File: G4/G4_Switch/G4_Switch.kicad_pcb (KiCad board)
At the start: 2 copper layers, 70.5 x 91.4 mm, 28 parts, among them J1 Conn_01x09_Socket, J2 Conn_01x09_Socket, J3 DB25_Plug, U1 NUCLEO-G491RE, U2 74HC594, U3 74HC594, U4 ULN2003A, U5 ULN2003A

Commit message: updated G4_Switch
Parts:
- added C1: C, Capacitor_THT:C_Disc_D3.4mm_W2.1mm_P2.50mm, F.Cu at (115.0, 95.2)
- added C2: C, Capacitor_THT:C_Disc_D3.4mm_W2.1mm_P2.50mm, F.Cu at (141.0, 99.1)
- added J_GNDA1: Conn_01x01_Female, Connector_PinHeader_2.54mm:PinHeader_1x01_P2.54mm_Vertical, F.Cu at (161.3, 54.6)
- U1: footprint G4Lib:MODULE_NUCLEO-G491RE20 -> G4Lib:MODULE_NUCLEO-G491RE20noar
- moved JP4 38.0 mm to (115.6, 83.8)
- moved JP9 18.0 mm to (151.8, 86.4)
- moved JP8 15.1 mm to (151.8, 92.1)
- moved U5 12.9 mm to (140.3, 64.8), turned to 90 degrees
- moved JP3 12.0 mm to (115.6, 80.0)
- moved U4 10.5 mm to (113.7, 64.8), turned to 90 degrees
- moved JP1 10.2 mm to (115.6, 90.2)
- moved U2 8.28 mm to (129.5, 95.2)
- moved U3 4.62 mm to (143.5, 95.2)
- moved J1 4.49 mm to (109.2, 49.5)
- moved R_IDENT1 4.26 mm to (151.8, 96.5), turned to -90 degrees
- moved R_LED10 3.18 mm to (135.3, 115.6)
- moved R_LED4 3.18 mm to (115.6, 115.6)
- moved R_LED8 3.18 mm to (128.9, 115.6)
- moved R_LED2 3.17 mm to (109.2, 115.6)
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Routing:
- net S_CLR: track 0.00 -> 75.1 mm
- net GS13: track 73.5 -> 131.8 mm
- net GS12: track 70.3 -> 127.2 mm
- net S_VALID: track 0.00 -> 54.1 mm
- net GS8: track 88.9 -> 120.3 mm
- net GS7: track 86.1 -> 116.6 mm
- net GS9: track 95.1 -> 124.1 mm
- net GS10: track 100.8 -> 128.2 mm
- net GS11: track 107.8 -> 133.6 mm
- net Net-(U2-QH'): track 0.00 -> 21.1 mm
- net Net-(U2-QH): track 0.00 -> 20.5 mm
- net 3V3: track 42.5 -> 62.7 mm
- net GS1: track 26.6 -> 8.41 mm
- net GS0: track 27.6 -> 9.94 mm
- net Net-(U2-QA): track 23.0 -> 38.2 mm
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- added copper zone on B.Cu, net GND
- added copper zone on B.Cu, net GNDA
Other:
- board text added: "G4 Switch V1.0"
- board text removed: "Template G4 V2"

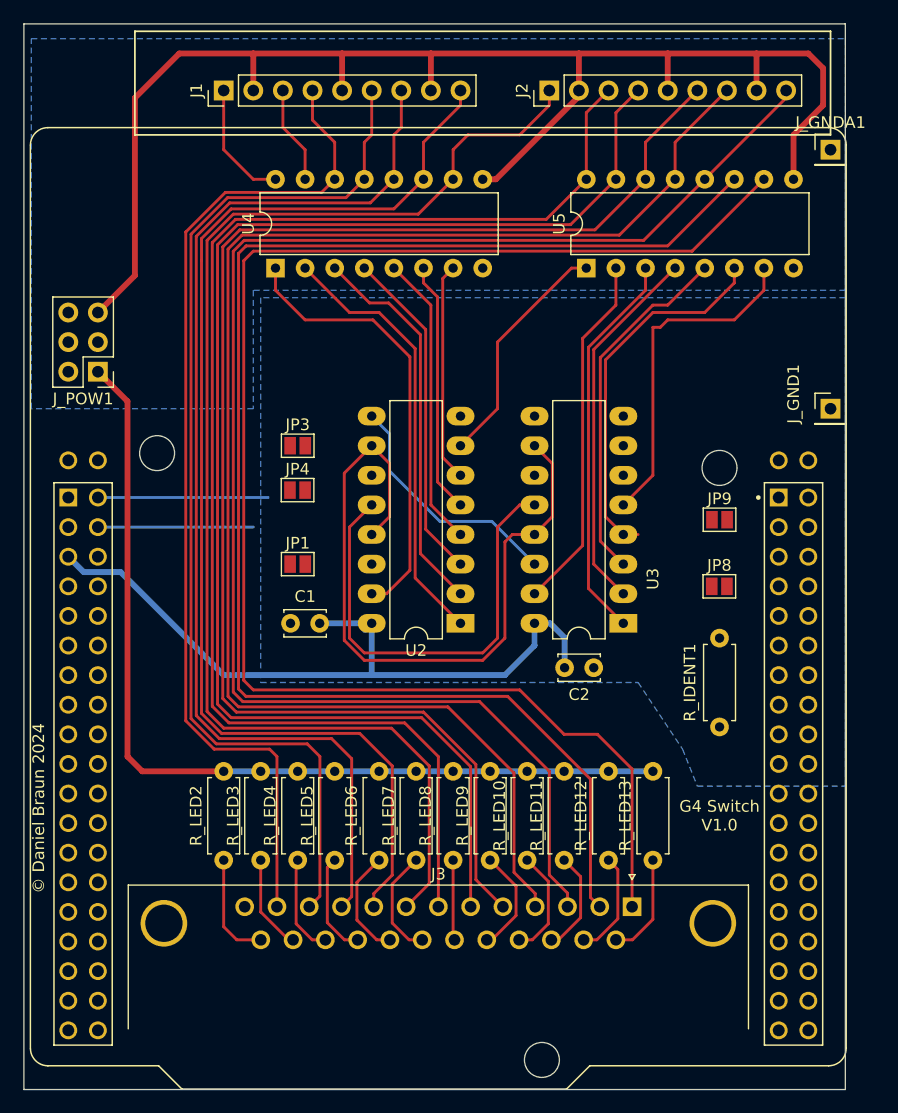
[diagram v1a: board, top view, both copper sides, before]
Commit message: updated G4_Switch, DRC run ok
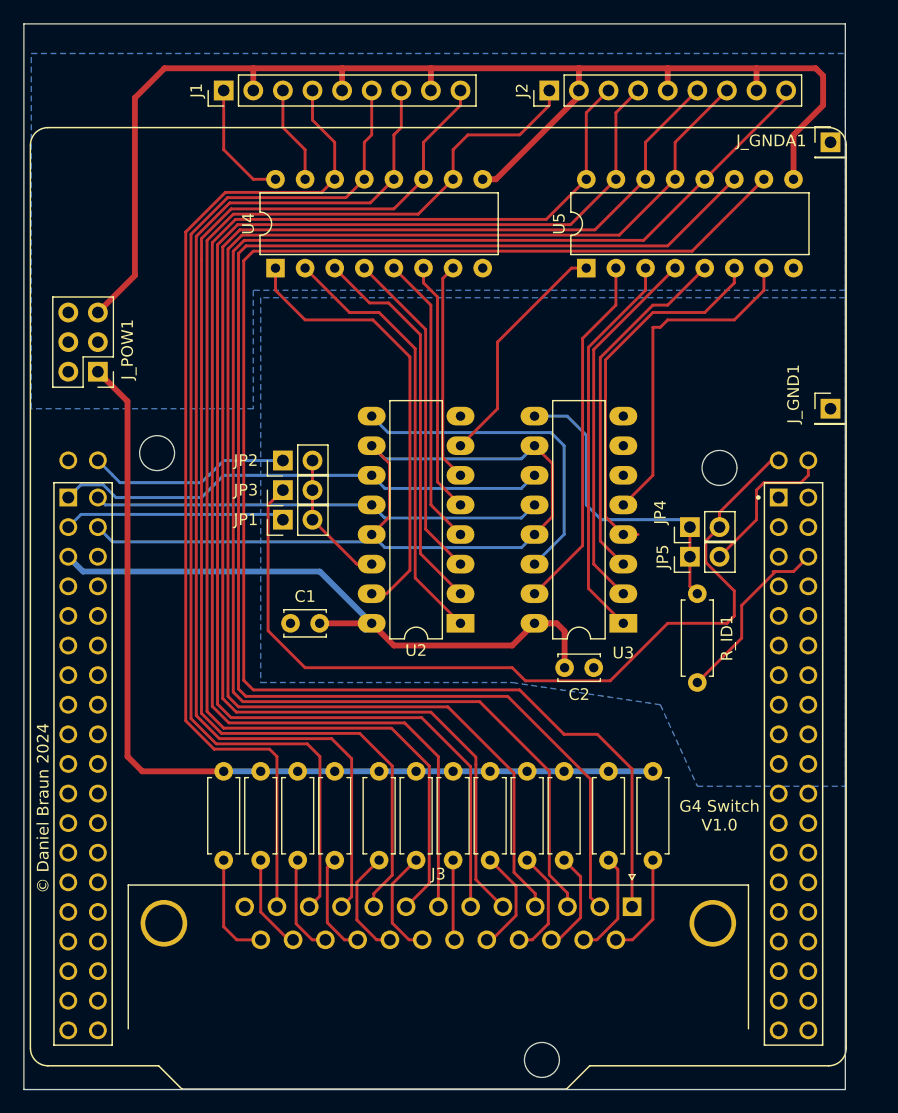
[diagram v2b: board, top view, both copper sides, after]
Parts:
- removed the JP3 at (115.6, 80.0)
- removed JP8, JP9: SolderJumper_2_Open, Jumper:SolderJumper-2_P1.3mm_Open_Pad1.0x1.5mm
- added JP2: SolderJumper_2_Open, Connector_PinHeader_2.54mm:PinHeader_1x02_P2.54mm_Vertical, F.Cu at (114.3, 81.3)
- added JP4: SolderJumper_2_Open, Connector_PinHeader_2.54mm:PinHeader_1x02_P2.54mm_Vertical, F.Cu at (149.2, 87.0)
- added JP5: SolderJumper_2_Open, Connector_PinHeader_2.54mm:PinHeader_1x02_P2.54mm_Vertical, F.Cu at (149.2, 89.5)
- JP1: footprint Jumper:SolderJumper-2_P1.3mm_Open_Pad1.0x1.5mm -> Connector_PinHeader_2.54mm:PinHeader_1x02_P2.54mm_Vertical
- JP3: renamed from JP4; footprint Jumper:SolderJumper-2_P1.3mm_Open_Pad1.0x1.5mm -> Connector_PinHeader_2.54mm:PinHeader_1x02_P2.54mm_Vertical
- moved R_ID1 4.26 mm to (149.9, 100.3), turned to 90 degrees
- moved JP1 4.02 mm to (114.3, 86.4), turned to 90 degrees
- moved JP3 1.26 mm to (114.3, 83.8), turned to 90 degrees
- moved J_GNDA1 0.63 mm to (161.3, 54.0)
- renumbered R_IDENT1 to R_ID1
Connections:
- U1 pad CN7_19: GND -> unconnected-(U1A-CN7_GND-PadCN7_19)
- U1 pad CN7_20: GND -> unconnected-(U1A-CN7_GND-PadCN7_20)
- U1 pad CN7_22: GND -> unconnected-(U1A-CN7_GND-PadCN7_22)
- U1 pad CN7_8: GND -> unconnected-(U1A-CN7_GND-PadCN7_8)
- U2 pad 11: SPI3_CLK -> SPI3_SCK
- U3 pad 11: SPI3_CLK -> SPI3_SCK
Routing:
- net SER2: track 0.00 -> 74.0 mm
- net SPI3_SCK: track 0.00 -> 42.6 mm
- net Net-(JP4-A): track 0.00 -> 26.8 mm
- net SPI3_MOSI: track 0.00 -> 19.1 mm
- net SER1: track 0.00 -> 17.5 mm
- net ASENSE: track 0.00 -> 16.1 mm
- net S_VALID: track 54.1 -> 38.7 mm
- net SER3: track 0.00 -> 13.3 mm
- net Net-(JP1-B): track 0.00 -> 11.7 mm
- net 12V: track 122.2 -> 113.2 mm
- net Net-(U2-QH'): track 21.1 -> 28.8 mm
- net 3V3: track 62.7 -> 56.6 mm
- net S_CLR: track 75.1 -> 71.9 mm
